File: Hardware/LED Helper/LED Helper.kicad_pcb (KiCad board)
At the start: 2 copper layers, 27.9 x 17.8 mm, 19 parts, among them J1 Conn_01x10, J2 Conn_01x10

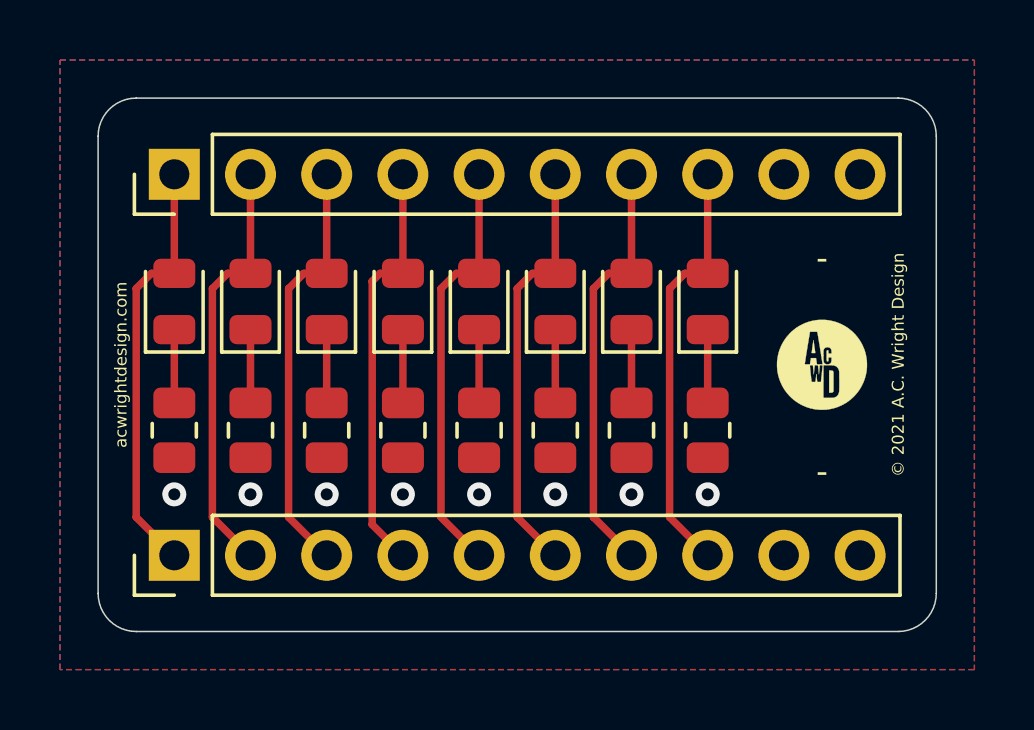
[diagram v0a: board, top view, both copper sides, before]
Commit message: Add switch helper
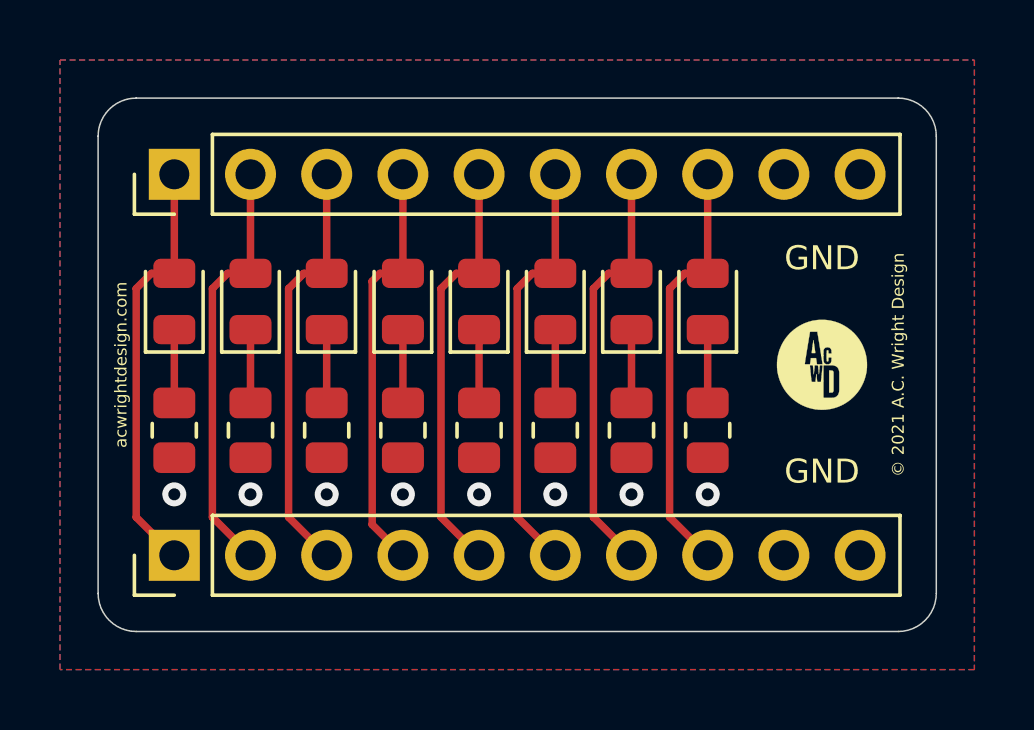
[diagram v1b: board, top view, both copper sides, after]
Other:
- board text added: "GND"
- board text removed: "-"
